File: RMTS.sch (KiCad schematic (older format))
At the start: 70 parts, among them J1 USB_B_Mini, J10 CONN_02, J11 CONN_02, J12 CONN_02, J2 Programmer, J3 Screw_Terminal_01x03, J4 Screw_Terminal_01x04, J5 Screw_Terminal_01x02, J6 Screw_Terminal_01x02, J7 Micro_SD_Card_Det_Hirose_DM3AT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

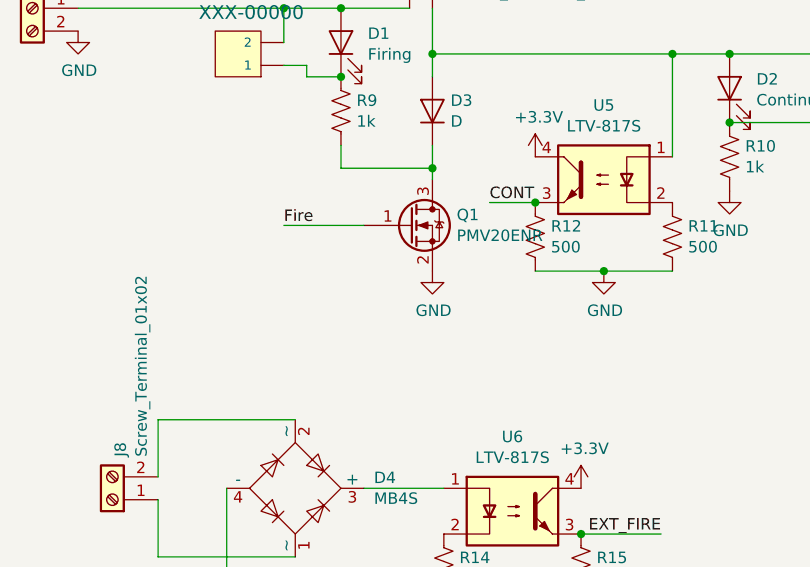
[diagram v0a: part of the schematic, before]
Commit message: Add pulldown to firing circuit
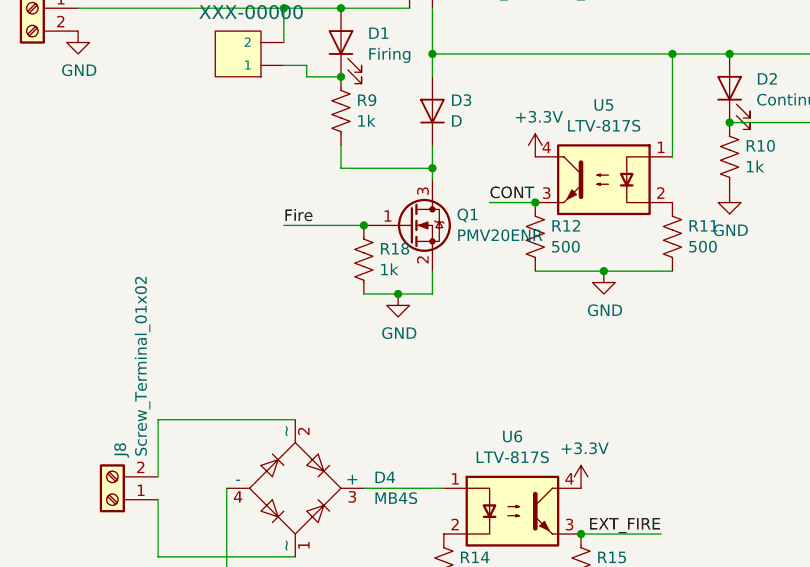
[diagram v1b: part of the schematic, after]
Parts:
- added R18: 1k, Resistor_SMD:R_0805_2012Metric_Pad1.15x1.40mm_HandSolder, symbol Device:R_US
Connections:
- net Fire: now also R18.1
- net GND: now also R18.2
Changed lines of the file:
@@
 Connection ~ 1700 1250
-Wire Wire Line
-	1700 1250 2150 1250
 Wire Wire Line
 	1700 1100 1900 1100
@@
 L power:GND #PWR0134
 U 1 1 5D485AAA
-P 13350 6600
-F 0 "#PWR0134" H 13350 6350 50  0001 C CNN
-F 1 "GND" H 13355 6427 50  0000 C CNN
-F 2 "" H 13350 6600 50  0001 C CNN
-F 3 "" H 13350 6600 50  0001 C CNN
-	1    13350 6600
+P 13200 6700
+F 0 "#PWR0134" H 13200 6450 50  0001 C CNN
+F 1 "GND" H 13205 6527 50  0000 C CNN
+F 2 "" H 13200 6700 50  0001 C CNN
+F 3 "" H 13200 6700 50  0001 C CNN
+	1    13200 6700
 	1    0    0    -1
 $EndComp
@@
 	11400 4800 11050 4800
 Connection ~ 11050 4800
+Wire Wire Line
+	1700 1250 2150 1250
+$Comp
+L Device:R_US R18
+U 1 1 5EC9847F
+P 13050 6550
+F 0 "R18" H 13118 6596 50  0000 L CNN
+F 1 "1k" H 13118 6505 50  0000 L CNN
+F 2 "Resistor_SMD:R_0805_2012Metric_Pad1.15x1.40mm_HandSolder" V 13090 6540 50  0001 C CNN
+F 3 "~" H 13050 6550 50  0001 C CNN
+	1    13050 6550
+	1    0    0    -1
+$EndComp
+Connection ~ 13050 6400
+Wire Wire Line
+	13050 6700 13200 6700
+Wire Wire Line
+	13350 6600 13350 6700
+Wire Wire Line
+	13350 6700 13200 6700
+Connection ~ 13200 6700
 $EndSCHEMATC

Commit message: Add LCSC part numbers to components
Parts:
- C1: LCSC (none) -> C1779
- C10, C11, C12, C18, C3, C5, C6, C7, C8: LCSC (none) -> C49678
- C13: LCSC (none) -> C15850
- C14, C15: LCSC (none) -> C1792
- C17: LCSC (none) -> C13967
- C4, C9: LCSC (none) -> C49217
- D1, D2, D5, D6: LCSC (none) -> C84256
- D3: LCSC (none) -> C96515
- D4: LCSC (none) -> C151727
- L1: LCSC (none) -> C1042
- R1, R2: LCSC (none) -> C17634
- R10, R16, R17, R18, R4, R6, R7, R8, R9: LCSC (none) -> C17513
- R11, R12, R13, R14, R15: LCSC (none) -> C17734
- R3: LCSC (none) -> C17710
- R5: LCSC (none) -> C17721
- U1: LCSC (none) -> C143875
- U5, U6: LCSC (none) -> C22113

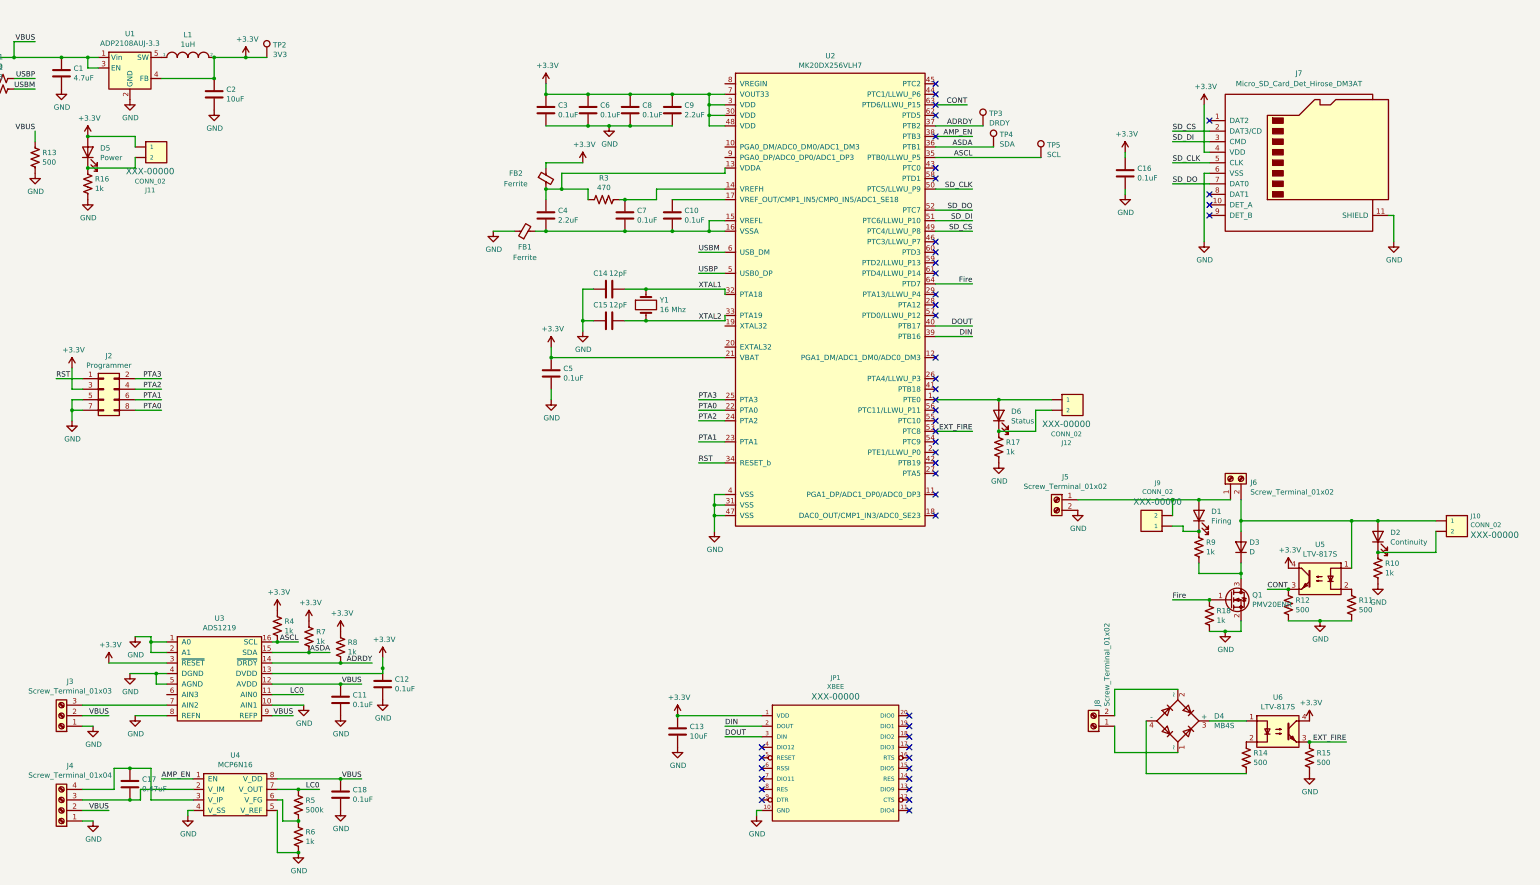
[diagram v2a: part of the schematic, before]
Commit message: Made external LED channels separate from onboard LEDs
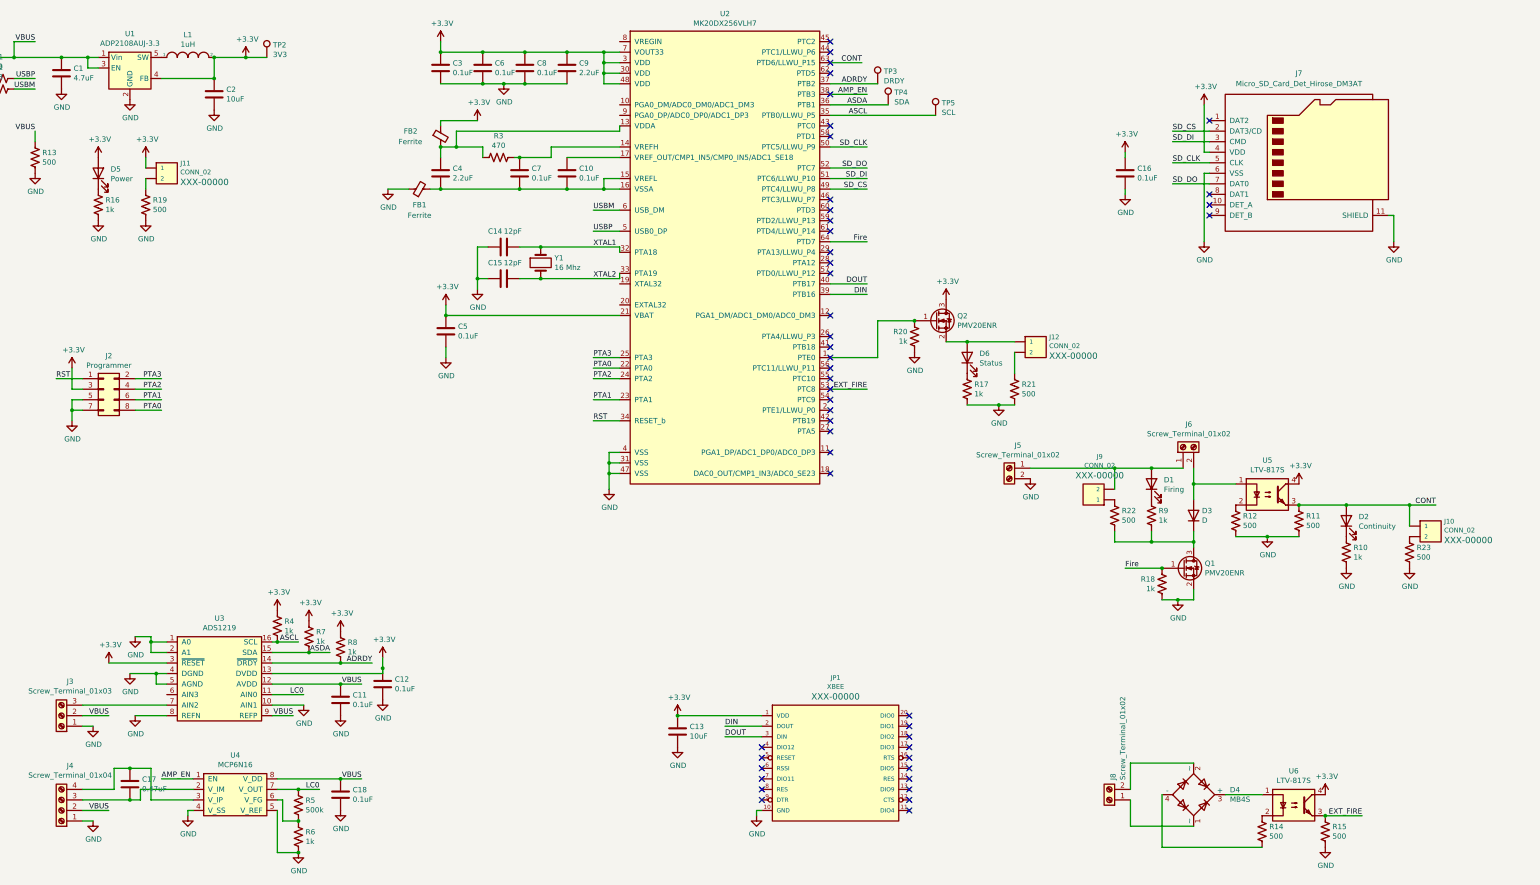
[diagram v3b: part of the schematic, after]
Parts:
- added Q2: PMV20ENR, Package_TO_SOT_SMD:SOT-23, symbol Transistor_FET:DMG3402L
- added R19, R21, R22, R23: 500, Resistor_SMD:R_0805_2012Metric_Pad1.15x1.40mm_HandSolder, symbol Device:R_US
- added R20: 1k, Resistor_SMD:R_0805_2012Metric_Pad1.15x1.40mm_HandSolder, symbol Device:R_US
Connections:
- net +3V3: now also Q2.3 (D)
- net CONT: now also D2.2 (A), J10.1, R11.1; no longer R12.1
- net GND: now also R19.2, R20.2, R21.2, R23.2
- net at D6.2 (A), J12.1: now also Q2.2 (S); no longer U2.1 (PTE0)
- net at D3.1 (K), Q1.3 (D), R9.2: now also R22.2
- net at D3.2 (A), J6.2 (Pin_2), U5.1: no longer D2.2 (A), J10.1
- net at D2.1 (K), R10.1: no longer J10.2
- net at D1.1 (K), R9.1: no longer J9.1
- net at U5.2: now also R12.1; no longer R11.1
- net at D5.1 (K), R16.1: no longer J11.2
- net at D6.1 (K), R17.1: no longer J12.2
- new net: Q2.1 (G), R20.1, U2.1 (PTE0)
- new net: J9.1, R22.1
- new net: J10.2, R23.1
- new net: J11.2, R19.1
- new net: J12.2, R21.1
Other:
- moved on the sheet: C10, C14, C15, C3, C4, C5, C6, C7, C8, C9, D1, D2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

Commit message: Decrease keepalive resistor value
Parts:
- R13: value 500 -> 330
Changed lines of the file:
@@
 P 1900 2200
 F 0 "R13" H 1968 2246 50  0000 L CNN
-F 1 "500" H 1968 2155 50  0000 L CNN
+F 1 "330" H 1968 2155 50  0000 L CNN
 F 2 "Resistor_SMD:R_0805_2012Metric_Pad1.15x1.40mm_HandSolder" V 1940 2190 50  0001 C CNN
 F 3 "~" H 1900 2200 50  0001 C CNN

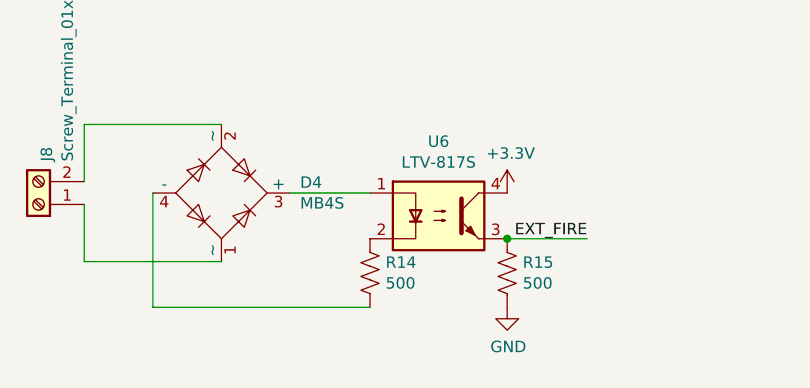
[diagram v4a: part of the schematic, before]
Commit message: Increase resistance of trigger circuit
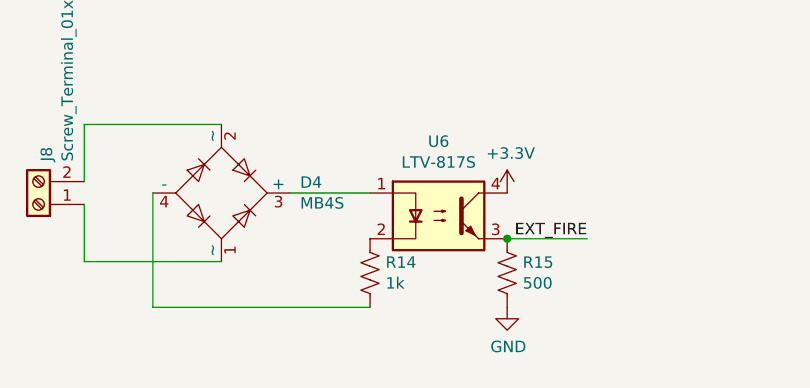
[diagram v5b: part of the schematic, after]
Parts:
- R14: value 500 -> 1k
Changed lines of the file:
@@
 P 13550 8600
 F 0 "R14" H 13618 8646 50  0000 L CNN
-F 1 "500" H 13618 8555 50  0000 L CNN
+F 1 "1k" H 13618 8555 50  0000 L CNN
 F 2 "Resistor_SMD:R_0805_2012Metric_Pad1.15x1.40mm_HandSolder" V 13590 8590 50  0001 C CNN
 F 3 "~" H 13550 8600 50  0001 C CNN

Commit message: Improve amplifier circuit
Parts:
- removed TP3: DRDY, TestPoint:TestPoint_THTPad_1.0x1.0mm_Drill0.5mm, symbol Connector:TestPoint
- removed TP4: SDA, TestPoint:TestPoint_THTPad_1.0x1.0mm_Drill0.5mm, symbol Connector:TestPoint
- removed TP5: SCL, TestPoint:TestPoint_THTPad_1.0x1.0mm_Drill0.5mm, symbol Connector:TestPoint
- added C19: 4.7uF, Capacitor_SMD:C_0805_2012Metric_Pad1.15x1.40mm_HandSolder, symbol Device:C
- added R24, R25: 1k, Resistor_SMD:R_0805_2012Metric_Pad1.15x1.40mm_HandSolder, symbol Device:R_US
- added U7: LM4040DBZ-2.5, Package_TO_SOT_SMD:SOT-23, symbol Reference_Voltage:LM4040DBZ-2.5
- R5: value 500k -> 250k
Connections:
- net AMP_EN: no longer U4.1 (EN)
- net GND: now also C19.2, U7.2 (A); no longer R6.2, U4.5 (V_REF)
- net VBUS: now also U4.1 (EN), C19.1, R25.1
- new net: R24.1, U4.5 (V_REF)
- new net: R24.2, R25.2, R6.2, U7.1 (K)
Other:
- moved on the sheet: C18, R5, R6
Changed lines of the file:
@@
 Wire Wire Line
 	2800 7100 3050 7100
-Text Label 9800 1800 2    50   ~ 0
+Text Label 10450 1800 2    50   ~ 0
 ASCL
-Text Label 9800 1700 2    50   ~ 0
+Text Label 10000 1700 2    50   ~ 0
 ASDA
-Text Label 9800 1500 2    50   ~ 0
+Text Label 9900 1500 2    50   ~ 0
 ADRDY
 $Comp
@@
 Text Label 9800 1600 2    50   ~ 0
 AMP_EN
-$Comp
-L Connector:TestPoint TP3
-U 1 1 5D79BB5E
-P 9900 1500
-F 0 "TP3" H 9958 1618 50  0000 L CNN
-F 1 "DRDY" H 9958 1527 50  0000 L CNN
-F 2 "TestPoint:TestPoint_THTPad_1.0x1.0mm_Drill0.5mm" H 10100 1500 50  0001 C CNN
-F 3 "~" H 10100 1500 50  0001 C CNN
-	1    9900 1500
-	1    0    0    -1
-$EndComp
-$Comp
-L Connector:TestPoint TP4
-U 1 1 5D79EB42
-P 10000 1700
-F 0 "TP4" H 10058 1818 50  0000 L CNN
-F 1 "SDA" H 10058 1727 50  0000 L CNN
-F 2 "TestPoint:TestPoint_THTPad_1.0x1.0mm_Drill0.5mm" H 10200 1700 50  0001 C CNN
-F 3 "~" H 10200 1700 50  0001 C CNN
-	1    10000 1700
-	1    0    0    -1
-$EndComp
-$Comp
-L Connector:TestPoint TP5
-U 1 1 5D79F9A3
-P 10450 1800
-F 0 "TP5" H 10508 1918 50  0000 L CNN
-F 1 "SCL" H 10508 1827 50  0000 L CNN
-F 2 "TestPoint:TestPoint_THTPad_1.0x1.0mm_Drill0.5mm" H 10650 1800 50  0001 C CNN
-F 3 "~" H 10650 1800 50  0001 C CNN
-	1    10450 1800
-	1    0    0    -1
-$EndComp
 Wire Wire Line
 	9450 1500 9900 1500
 Wire Wire Line
 	9450 1700 10000 1700
-Wire Wire Line
-	9450 1800 10450 1800
 Wire Wire Line
 	4150 7500 4350 7500
@@
 	11350 5150 12150 5150
 Wire Wire Line
-	4400 8200 4600 8200
-Connection ~ 4400 8200
-Text Label 4600 8200 2    50   ~ 0
+	4650 8200 4850 8200
+Connection ~ 4650 8200
+Text Label 4850 8200 2    50   ~ 0
 LC0
-Wire Wire Line
-	4200 8200 4400 8200
-Connection ~ 4400 8500
+Connection ~ 4650 8500
 Wire Wire Line
 	4250 8300 4200 8300
 Wire Wire Line
 	4250 8500 4250 8300
-Wire Wire Line
-	4400 8500 4250 8500
 $Comp
 L Device:R_US R6
 U 1 1 5E5AA280
-P 4400 8650
-F 0 "R6" H 4468 8696 50  0000 L CNN
-F 1 "1k" H 4468 8605 50  0000 L CNN
-F 2 "Resistor_SMD:R_0805_2012Metric_Pad1.15x1.40mm_HandSolder" V 4440 8640 50  0001 C CNN
-F 3 "~" H 4400 8650 50  0001 C CNN
-F 4 "C17513" H 4400 8650 50  0001 C CNN "LCSC"
-	1    4400 8650
+P 4650 8650
+F 0 "R6" H 4718 8696 50  0000 L CNN
+F 1 "1k" H 4718 8605 50  0000 L CNN
+F 2 "Resistor_SMD:R_0805_2012Metric_Pad1.15x1.40mm_HandSolder" V 4690 8640 50  0001 C CNN
+F 3 "~" H 4650 8650 50  0001 C CNN
+F 4 "C17513" H 4650 8650 50  0001 C CNN "LCSC"
+	1    4650 8650
 	1    0    0    -1
 $EndComp
@@
 L Device:R_US R5
 U 1 1 5E5A9716
-P 4400 8350
-F 0 "R5" H 4468 8396 50  0000 L CNN
-F 1 "500k" H 4468 8305 50  0000 L CNN
-F 2 "Resistor_SMD:R_0805_2012Metric_Pad1.15x1.40mm_HandSolder" V 4440 8340 50  0001 C CNN
-F 3 "~" H 4400 8350 50  0001 C CNN
-F 4 " C17721" H 4400 8350 50  0001 C CNN "LCSC"
-	1    4400 8350
+P 4650 8350
+F 0 "R5" H 4718 8396 50  0000 L CNN
+F 1 "250k" H 4718 8305 50  0000 L CNN
+F 2 "Resistor_SMD:R_0805_2012Metric_Pad1.15x1.40mm_HandSolder" V 4690 8340 50  0001 C CNN
+F 3 "~" H 4650 8350 50  0001 C CNN
+F 4 " C17721" H 4650 8350 50  0001 C CNN "LCSC"
+	1    4650 8350
 	1    0    0    -1
 $EndComp
@@
 L power:GND #PWR0124
 U 1 1 5E59AFE5
-P 4400 8800
-F 0 "#PWR0124" H 4400 8550 50  0001 C CNN
-F 1 "GND" H 4405 8627 50  0000 C CNN
-F 2 "" H 4400 8800 50  0001 C CNN
-F 3 "" H 4400 8800 50  0001 C CNN
-	1    4400 8800
+P 5250 9400
+F 0 "#PWR0124" H 5250 9150 50  0001 C CNN
+F 1 "GND" H 5255 9227 50  0000 C CNN
+F 2 "" H 5250 9400 50  0001 C CNN
+F 3 "" H 5250 9400 50  0001 C CNN
+	1    5250 9400
 	1    0    0    -1
 $EndComp
@@
 	1    0    0    -1
 $EndComp
-Text Label 5000 8100 2    50   ~ 0
+Text Label 5700 8100 2    50   ~ 0
 VBUS
-Wire Wire Line
-	3100 8100 3400 8100
-Text Label 3100 8100 0    50   ~ 0
-AMP_EN
 $Comp
 L Mine:MCP6N16 U4
@@
 Wire Wire Line
 	3000 8300 3400 8300
-Wire Wire Line
-	4400 8800 4200 8800
-Wire Wire Line
-	4200 8800 4200 8400
-Connection ~ 4400 8800
 $Comp
 L Device:C C18
 U 1 1 5E6DE71A
-P 4800 8250
-F 0 "C18" H 4915 8296 50  0000 L CNN
-F 1 "0.1uF" H 4915 8205 50  0000 L CNN
-F 2 "Capacitor_SMD:C_0805_2012Metric_Pad1.15x1.40mm_HandSolder" H 4838 8100 50  0001 C CNN
-F 3 "~" H 4800 8250 50  0001 C CNN
-F 4 " C49678" H 4800 8250 50  0001 C CNN "LCSC"
-	1    4800 8250
-	1    0    0    -1
-$EndComp
-Wire Wire Line
-	4200 8100 4800 8100
-Wire Wire Line
-	4800 8100 5000 8100
-Connection ~ 4800 8100
-$Comp
-L power:GND #PWR0126
-U 1 1 5E6F8F4A
-P 4800 8400
-F 0 "#PWR0126" H 4800 8150 50  0001 C CNN
-F 1 "GND" H 4805 8227 50  0000 C CNN
-F 2 "" H 4800 8400 50  0001 C CNN
-F 3 "" H 4800 8400 50  0001 C CNN
-	1    4800 8400
-	1    0    0    -1
-$EndComp
+P 5050 8250
+F 0 "C18" H 5165 8296 50  0000 L CNN
+F 1 "0.1uF" H 5165 8205 50  0000 L CNN
+F 2 "Capacitor_SMD:C_0805_2012Metric_Pad1.15x1.40mm_HandSolder" H 5088 8100 50  0001 C CNN
+F 3 "~" H 5050 8250 50  0001 C CNN
+F 4 " C49678" H 5050 8250 50  0001 C CNN "LCSC"
+	1    5050 8250
+	1    0    0    -1
+$EndComp
+Connection ~ 5050 8100
 $Comp
 L Diode_Bridge:MB4S D4
@@
 Wire Wire Line
 	11200 4050 11200 4250
+Wire Wire Line
+	4200 8100 5050 8100
+Wire Wire Line
+	4200 8200 4650 8200
+Wire Wire Line
+	4250 8500 4650 8500
+Wire Wire Line
+	4200 8400 4200 8500
+Wire Wire Line
+	4200 8800 4650 8800
+$Comp
+L Device:R_US R25
+U 1 1 5FF22571
+P 5250 8950
+F 0 "R25" H 5318 8996 50  0000 L CNN
+F 1 "1k" H 5318 8905 50  0000 L CNN
+F 2 "Resistor_SMD:R_0805_2012Metric_Pad1.15x1.40mm_HandSolder" V 5290 8940 50  0001 C CNN
+F 3 "~" H 5250 8950 50  0001 C CNN
+F 4 "C17513" H 5250 8950 50  0001 C CNN "LCSC"
+	1    5250 8950
+	1    0    0    -1
+$EndComp
+Text Label 5250 8800 2    50   ~ 0
+VBUS
+$Comp
+L Device:C C19
+U 1 1 5FF42F16
+P 5500 8250
+F 0 "C19" H 5615 8296 50  0000 L CNN
+F 1 "4.7uF" H 5615 8205 50  0000 L CNN
+F 2 "Capacitor_SMD:C_0805_2012Metric_Pad1.15x1.40mm_HandSolder" H 5538 8100 50  0001 C CNN
+F 3 "~" H 5500 8250 50  0001 C CNN
+F 4 " C49678" H 5500 8250 50  0001 C CNN "LCSC"
+	1    5500 8250
+	1    0    0    -1
+$EndComp
+Wire Wire Line
+	5050 8100 5500 8100
+Connection ~ 5500 8100
+Wire Wire Line
+	5500 8100 5700 8100
+$Comp
+L power:GND #PWR0126
+U 1 1 5FF83C8C
+P 5250 8400
+F 0 "#PWR0126" H 5250 8150 50  0001 C CNN
+F 1 "GND" H 5255 8227 50  0000 C CNN
+F 2 "" H 5250 8400 50  0001 C CNN
+F 3 "" H 5250 8400 50  0001 C CNN
+	1    5250 8400
+	1    0    0    -1
+$EndComp
+Wire Wire Line
+	5050 8400 5250 8400
+Wire Wire Line
+	5500 8400 5250 8400
+Connection ~ 5250 8400
+$Comp
+L Reference_Voltage:LM4040DBZ-2.5 U7
+U 1 1 5FFB4185
+P 5250 9250
+F 0 "U7" V 5296 9162 50  0000 R CNN
+F 1 "LM4040DBZ-2.5" V 5205 9162 50  0000 R CNN
+F 2 "Package_TO_SOT_SMD:SOT-23" H 5250 9050 50  0001 C CIN
+F 3 "http://www.ti.com/lit/ds/symlink/lm4040-n.pdf" H 5250 9250 50  0001 C CIN
+	1    5250 9250
+	0    -1   -1   0
+$EndComp
+Wire Wire Line
+	4650 8800 4950 8800
+Wire Wire Line
+	4950 8800 4950 9100
+Wire Wire Line
+	4950 9100 5250 9100
+Connection ~ 4650 8800
+Connection ~ 5250 9100
+$Comp
+L Device:R_US R24
+U 1 1 600453A9
+P 4200 8650
+F 0 "R24" H 4268 8696 50  0000 L CNN
+F 1 "1k" H 4268 8605 50  0000 L CNN
+F 2 "Resistor_SMD:R_0805_2012Metric_Pad1.15x1.40mm_HandSolder" V 4240 8640 50  0001 C CNN
+F 3 "~" H 4200 8650 50  0001 C CNN
+F 4 "C17513" H 4200 8650 50  0001 C CNN "LCSC"
+	1    4200 8650
+	1    0    0    -1
+$EndComp
+Wire Wire Line
+	9450 1800 10450 1800
+Text Label 3400 8100 2    50   ~ 0
+VBUS
 $EndSCHEMATC
